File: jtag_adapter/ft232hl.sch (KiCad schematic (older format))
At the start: 29 parts, among them U1 N.F./93AA56BT-I/OT, U2 FT232HL, Y1 12MHz

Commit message: wip
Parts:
- removed C4: 24pF, Capacitor_SMD:C_0603_1608Metric, symbol Device:C
- removed C5: 12pF, Capacitor_SMD:C_0603_1608Metric, symbol Device:C
- removed JP1: Jumper, Jumper:SolderJumper-2_P1.3mm_Bridged_Pad1.0x1.5mm, symbol Device:Jumper
- removed Y1: 12MHz, Crystal:Crystal_SMD_SeikoEpson_FA238-4Pin_3.2x2.5mm, symbol Device:Crystal_GND24
- added C3: 0.1uF, Capacitor_SMD:C_0603_1608Metric, symbol Device:C
- added D3: JTAG_ACT, LED_SMD:LED_0603_1608Metric, symbol Device:LED
- added R14: 1k, Resistor_SMD:R_0603_1608Metric, symbol Device:R
- added R8: 10k, Resistor_SMD:R_0603_1608Metric, symbol Device:R
- added U2: SIT2001B, Package_TO_SOT_SMD:SOT-23-5, symbol sit2001:SIT2001B
- C4: renamed from C3; value 0.01uF -> 0.1uF
- R12: renamed from R7; value 10k -> 100k; MPN RC0603FR-0710KL -> (none)
- renumbered C11 to C10, C12 to C11, C13 to C12, C14 to C13, C15 to C14, C16 to C15, C17 to C16, C18 to C17, C6 to C5, C7 to C6, C8 to C7, C9 to C8, C10 to C9, L2 to L3, L3 to L4, R5 to R10, R6 to R11, R8 to R13, R3 to R7, R4 to R9, U2 to U3
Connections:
- net +3V3: now also C3.1, R14.2, R8.2, U2.4 (VDD)
- net GND: now also C3.2, U2.1 (GND)
- net JTAG_nSRST: now also U3.31 (ACBUS7); no longer U3.17 (ADBUS4)
- net JTAG_nTRST: now also U3.32 (ACBUS8); no longer U3.18 (ADBUS5)
- net XCSI: now reaches U3.1 (XCSI)
- net XCSI: now also U2.5 (OUT)
- net XCSO: now reaches U3.2 (XCSO)
- net SWD_EN: now reaches U3.28 (ACBUS4)
- net JTAG_EN: now reaches U3.29 (ACBUS5)
- net SWDIO_OE: now reaches U3.30 (ACBUS6)
- net JTAG_ACT_LED: now reaches U3.33 (ACBUS9)
- net JTAG_ACT_LED: now also D3.1 (K)
- new net: R8.1, U2.3 (OE)
- new net: D3.2 (A), R14.1
- no-connect marks 11 -> 8

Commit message: wip
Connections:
- net JTAG_ACT_LED: now also U3.31 (ACBUS7); no longer U3.33 (ACBUS9)
- net JTAG_nSRST: now also U3.32 (ACBUS8); no longer U3.31 (ACBUS7)
- net JTAG_nTRST: now also U3.33 (ACBUS9); no longer U3.32 (ACBUS8)
- net ~RESET: now reaches C4.1, R12.1, U3.34 (~RESET)
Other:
- note added: "ACBUS8 & 9 are connected \nto an internal pull-up resistor."
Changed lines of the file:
@@
 Text HLabel 7900 2800 2    50   Input ~ 0
 JTAG_TMS
-Text HLabel 7900 4100 2    50   Input ~ 0
+Text HLabel 7900 4200 2    50   Input ~ 0
 JTAG_nSRST
-Text HLabel 7900 4200 2    50   Input ~ 0
+Text HLabel 7900 4300 2    50   Input ~ 0
 JTAG_nTRST
 Text HLabel 7900 3200 2    50   Input ~ 0
@@
 Wire Wire Line
 	1650 4000 1650 4200
-Text Label 7900 4300 0    50   ~ 0
+Text Label 7900 4100 0    50   ~ 0
 JTAG_ACT_LED
 Text HLabel 7900 3800 2    50   Input ~ 0
@@
 NoConn ~ 7100 3600
 NoConn ~ 7100 3700
+Text Label 5050 3400 0    50   ~ 0
+~RESET
+Text Notes 7050 4550 0    50   ~ 0
+ACBUS8 & 9 are connected \nto an internal pull-up resistor.
 $EndSCHEMATC

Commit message: v1.0 基板発注
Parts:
- removed D3: JTAG_ACT, LED_SMD:LED_0603_1608Metric, symbol Device:LED
- removed R14: 1k, Resistor_SMD:R_0603_1608Metric, symbol Device:R
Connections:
- net JTAG_EN: now also U3.28 (ACBUS4); no longer U3.29 (ACBUS5)
- net JTAG_nSRST: now also U3.33 (ACBUS9); no longer U3.32 (ACBUS8)
- net JTAG_nTRST: now also U3.32 (ACBUS8); no longer U3.33 (ACBUS9)
- net SWD_EN: now also U3.29 (ACBUS5); no longer U3.28 (ACBUS4)
- net JTAG_ACT_LED: no longer names the net of U3.31 (ACBUS7)
- no-connect marks 8 -> 9
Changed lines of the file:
@@
 Text HLabel 7900 2800 2    50   Input ~ 0
 JTAG_TMS
+Text HLabel 7900 4300 2    50   Input ~ 0
+JTAG_nSRST
 Text HLabel 7900 4200 2    50   Input ~ 0
-JTAG_nSRST
-Text HLabel 7900 4300 2    50   Input ~ 0
 JTAG_nTRST
 Text HLabel 7900 3200 2    50   Input ~ 0
@@
 Wire Wire Line
 	1650 4000 1650 4200
-Text Label 7900 4100 0    50   ~ 0
-JTAG_ACT_LED
+Text HLabel 7900 3900 2    50   Input ~ 0
+SWD_EN
 Text HLabel 7900 3800 2    50   Input ~ 0
-SWD_EN
-Wire Wire Line
-	10750 5600 10750 5700
-Wire Wire Line
-	10750 5200 10750 5300
-$Comp
-L Device:R R?
-U 1 1 615CF7DD
-P 10750 5450
-AR Path="/615CF7DD" Ref="R?"  Part="1"
-AR Path="/61247445/615CF7DD" Ref="R14"  Part="1"
-F 0 "R14" V 10850 5550 50  0000 C CNN
-F 1 "1k" V 10850 5350 50  0000 C CNN
-F 2 "Resistor_SMD:R_0603_1608Metric" V 10680 5450 50  0001 C CNN
-F 3 "~" H 10750 5450 50  0001 C CNN
-F 4 "RC0603FR-072KL" H 10750 5450 50  0001 C CNN "MPN"
-	1    10750 5450
-	-1   0    0    1
-$EndComp
-$Comp
-L Device:LED D?
-U 1 1 615CF7E3
-P 10750 5850
-AR Path="/615CF7E3" Ref="D?"  Part="1"
-AR Path="/61247445/615CF7E3" Ref="D3"  Part="1"
-F 0 "D3" V 10789 5732 50  0000 R CNN
-F 1 "JTAG_ACT" V 10698 5732 50  0000 R CNN
-F 2 "LED_SMD:LED_0603_1608Metric" H 10750 5850 50  0001 C CNN
-F 3 "~" H 10750 5850 50  0001 C CNN
-	1    10750 5850
-	0    -1   -1   0
-$EndComp
-Text Label 10600 6100 2    50   ~ 0
-JTAG_ACT_LED
-Text HLabel 7900 3900 2    50   Input ~ 0
 JTAG_EN
-$Comp
-L power:+3V3 #PWR?
-U 1 1 613CB40C
-P 10750 5200
-AR Path="/613CB40C" Ref="#PWR?"  Part="1"
-AR Path="/61247445/613CB40C" Ref="#PWR0101"  Part="1"
-F 0 "#PWR0101" H 10750 5050 50  0001 C CNN
-F 1 "+3V3" H 10765 5373 50  0000 C CNN
-F 2 "" H 10750 5200 50  0001 C CNN
-F 3 "" H 10750 5200 50  0001 C CNN
-	1    10750 5200
-	1    0    0    -1
-$EndComp
-Wire Wire Line
-	10750 6100 10750 6000
-Wire Wire Line
-	10750 6100 10600 6100
 Wire Notes Line
 	8800 700  8800 4350
@@
 	7900 4000 7100 4000
 Wire Wire Line
-	7100 4100 7900 4100
-Wire Wire Line
 	7900 4200 7100 4200
 Wire Wire Line
@@
 Text Notes 7050 4550 0    50   ~ 0
 ACBUS8 & 9 are connected \nto an internal pull-up resistor.
+NoConn ~ 7100 4100
 $EndSCHEMATC

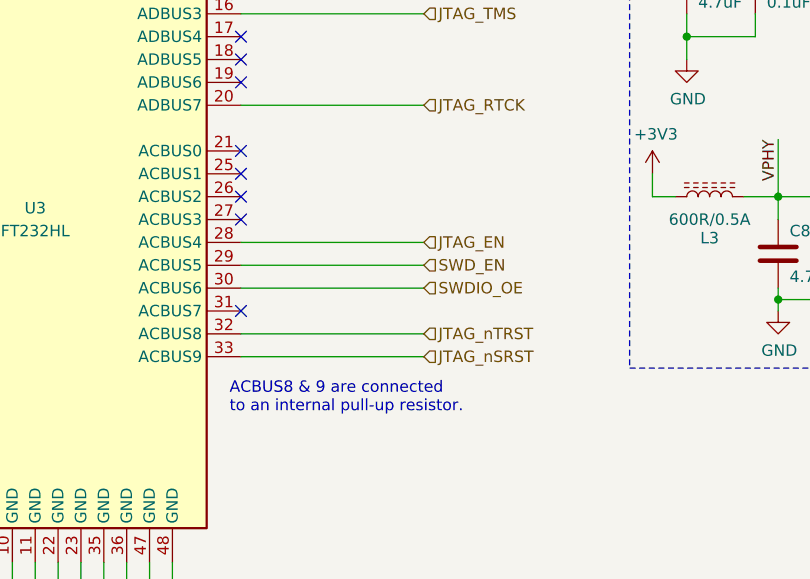
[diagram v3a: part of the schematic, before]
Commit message: wip: remove JTAG_EN pin
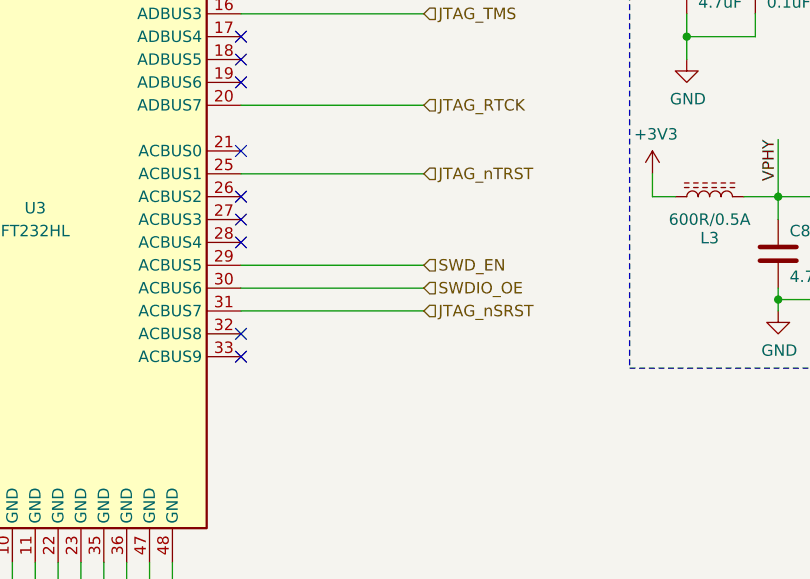
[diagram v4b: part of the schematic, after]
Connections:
- net JTAG_nSRST: now also U3.31 (ACBUS7); no longer U3.33 (ACBUS9)
- net JTAG_nTRST: now also U3.25 (ACBUS1); no longer U3.32 (ACBUS8)
- net JTAG_EN: no longer names the net of U3.28 (ACBUS4)
- no-connect marks 9 -> 10
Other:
- note removed: "ACBUS8 & 9 are connected \nto an internal pull-up resistor."
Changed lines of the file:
@@
 Text HLabel 7900 2800 2    50   Input ~ 0
 JTAG_TMS
-Text HLabel 7900 4300 2    50   Input ~ 0
+Text HLabel 7900 4100 2    50   Input ~ 0
 JTAG_nSRST
-Text HLabel 7900 4200 2    50   Input ~ 0
+Text HLabel 7900 3500 2    50   Input ~ 0
 JTAG_nTRST
 Text HLabel 7900 3200 2    50   Input ~ 0
@@
 Text HLabel 7900 3900 2    50   Input ~ 0
 SWD_EN
-Text HLabel 7900 3800 2    50   Input ~ 0
-JTAG_EN
 Wire Notes Line
 	8800 700  8800 4350
@@
 Wire Notes Line
 	11150 700  8800 700
+NoConn ~ 7100 2900
+NoConn ~ 7100 3000
+NoConn ~ 7100 3100
+Wire Wire Line
+	7100 3900 7900 3900
+Wire Wire Line
+	7900 4000 7100 4000
+NoConn ~ 7100 3400
+NoConn ~ 7100 3700
+NoConn ~ 7100 3600
+Text Label 5050 3400 0    50   ~ 0
+~RESET
 $Comp
 L Interface_USB:FT232H U?
@@
 	1    0    0    -1
 $EndComp
-NoConn ~ 7100 2900
-NoConn ~ 7100 3000
-NoConn ~ 7100 3100
-Wire Wire Line
-	7900 3800 7100 3800
-Wire Wire Line
-	7100 3900 7900 3900
-Wire Wire Line
-	7900 4000 7100 4000
-Wire Wire Line
-	7900 4200 7100 4200
-Wire Wire Line
-	7100 4300 7900 4300
-NoConn ~ 7100 3400
-NoConn ~ 7100 3500
-NoConn ~ 7100 3600
-NoConn ~ 7100 3700
-Text Label 5050 3400 0    50   ~ 0
-~RESET
-Text Notes 7050 4550 0    50   ~ 0
-ACBUS8 & 9 are connected \nto an internal pull-up resistor.
-NoConn ~ 7100 4100
+Wire Wire Line
+	7100 4100 7900 4100
+NoConn ~ 7100 4200
+NoConn ~ 7100 4300
+Wire Wire Line
+	7900 3500 7100 3500
+NoConn ~ 7100 3800
 $EndSCHEMATC
